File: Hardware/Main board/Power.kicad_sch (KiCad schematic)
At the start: 12 parts, among them U5 TLV1117-33, U6 TLV1117-33, U7 TLV1117-33, U8 TLV1117-33

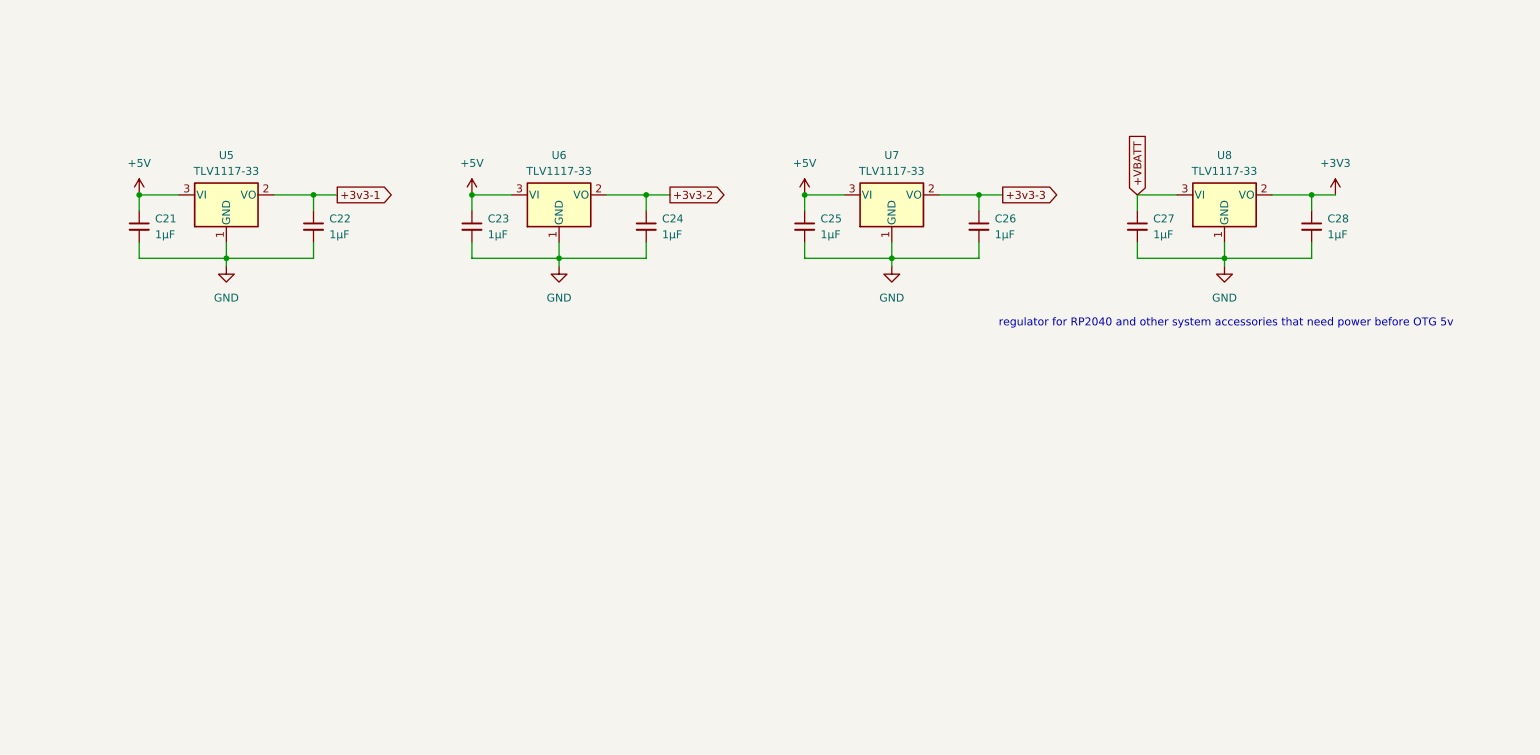
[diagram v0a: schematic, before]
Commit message: hardware changes and initial traces/layout
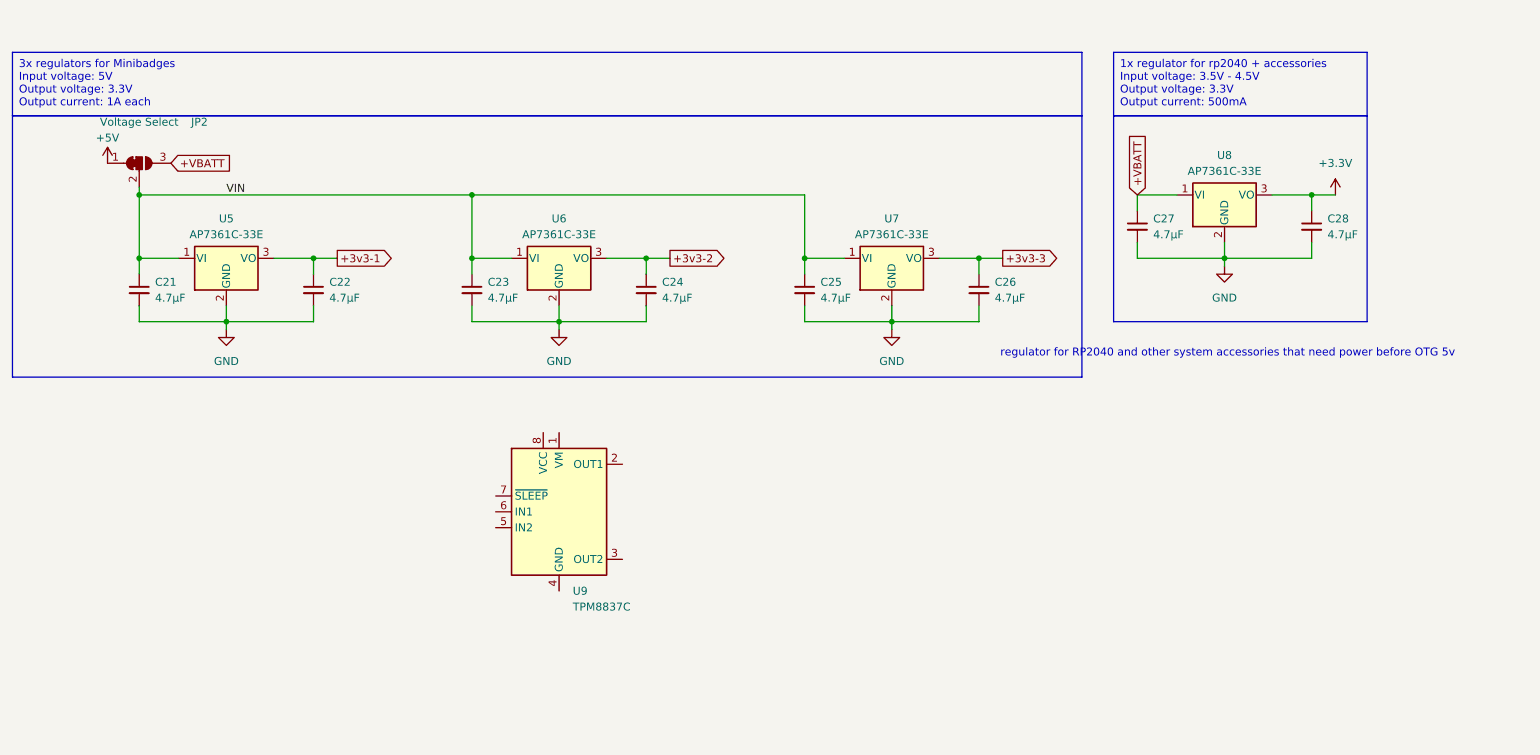
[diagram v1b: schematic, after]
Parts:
- added JP2: Voltage Select, Jumper:SolderJumper-3_P1.3mm_Bridged12_Pad1.0x1.5mm_NumberLabels, symbol Jumper:SolderJumper_3_Bridged12
- added U9: TPM8837C, Package_SO:SOIC-8_3.9x4.9mm_P1.27mm, symbol Driver_Motor:DRV8837C
- C21, C22, C23, C24, C25, C26, C27, C28: value 1μF -> 4.7μF; footprint (none) -> Capacitor_SMD:C_0603_1608Metric
- U5, U6, U7, U8: value TLV1117-33 -> AP7361C-33E; footprint (none) -> Package_TO_SOT_SMD:SOT-223-3_TabPin2; symbol Regulator_Linear:TLV1117-33 -> Regulator_Linear:AP7361C-33E
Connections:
- net +3v3-1: now also U5.3 (VO); no longer U5.2 (VO)
- net +3v3-2: now also U6.3 (VO); no longer U6.2 (VO)
- net +3v3-3: now also U7.3 (VO); no longer U7.2 (VO)
- net +5V: now also JP2.1 (A); no longer C21.1, C23.1, C25.1, U5.3 (VI), U6.3 (VI), U7.3 (VI)
- net +VBATT: now also U8.1 (VI), JP2.3 (B); no longer U8.3 (VI)
- net GND: now also U5.2 (GND), U6.2 (GND), U7.2 (GND), U8.2 (GND); no longer U5.1 (GND), U6.1 (GND), U7.1 (GND), U8.1 (GND)
- net +3V3 renamed +3.3V
- net +3.3V: now also U8.3 (VO); no longer U8.2 (VO)
- new net: U9.4 (GND), U9.9 (GND)
- new net VIN: C21.1, C23.1, C25.1, JP2.2 (C), U5.1 (VI), U6.1 (VI), U7.1 (VI)
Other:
- moved on the sheet: C21, C22, C23, C24, C25, C26, U5, U6, U7

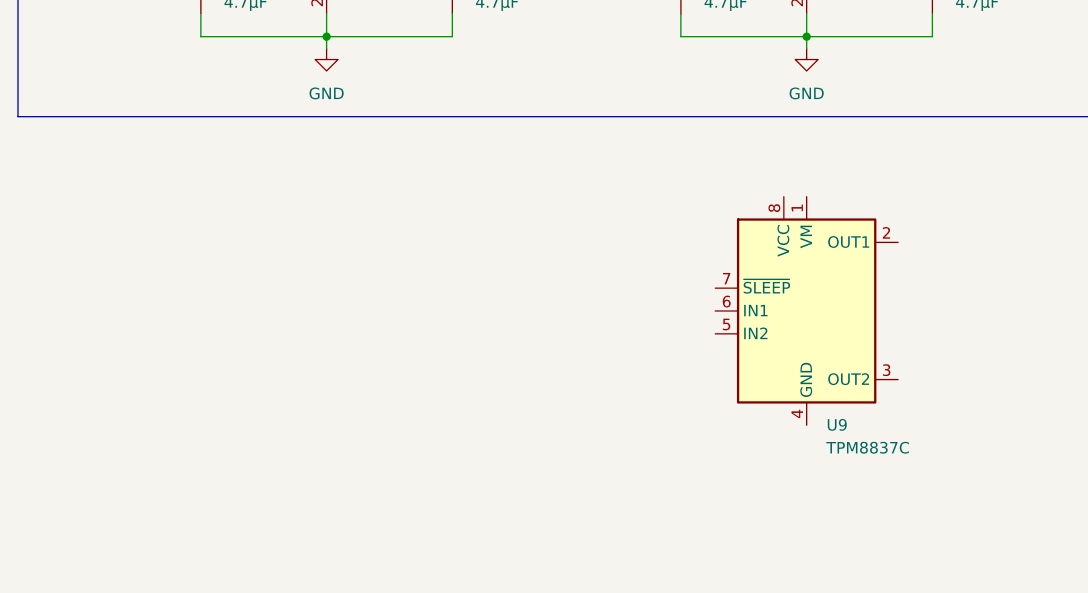
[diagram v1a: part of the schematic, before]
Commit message: update power for TPM
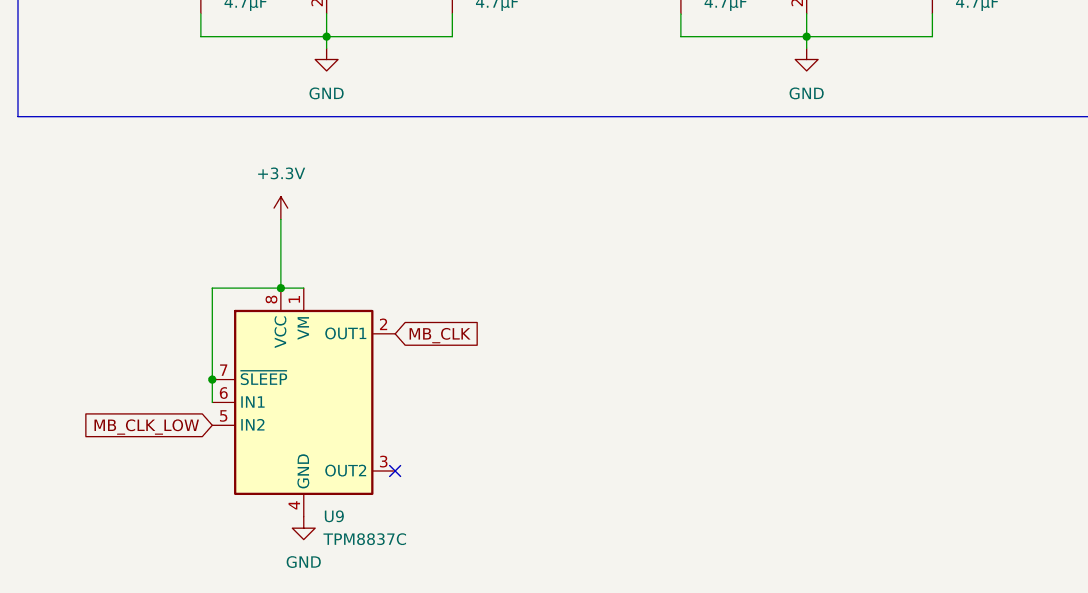
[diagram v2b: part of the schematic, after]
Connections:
- net +3.3V: now also U9.1 (VM), U9.6 (IN1), U9.7 (~{SLEEP}), U9.8 (VCC)
- net GND: now also U9.4 (GND), U9.9 (GND)
- net MB_CLK: now reaches U9.2 (OUT1)
- net MB_CLK_LOW: now reaches U9.5 (IN2)
- no-connect marks 0 -> 1
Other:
- moved on the sheet: U9
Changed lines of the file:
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@@
 	(paper "A4")
+	(junction
+		(at 49.53 113.03)
+		(diameter 0)
+		(color 0 0 0 0)
+	)
 	(junction
 		(at 129.54 64.77)
@@
 	)
 	(junction
+		(at 57.15 102.87)
+		(diameter 0)
+		(color 0 0 0 0)
+	)
+	(junction
 		(at 236.22 54.61)
 		(diameter 0)
@@
 		(color 0 0 0 0)
 	)
+	(no_connect
+		(at 69.85 123.19)
+	)
 	(wire
 		(pts
@@
 	(wire
 		(pts
+			(xy 49.53 113.03) (xy 49.53 115.57)
+		)
+		(stroke
+			(width 0)
+			(type default)
+		)
+	)
+	(wire
+		(pts
 			(xy 208.28 64.77) (xy 222.25 64.77)
 		)
@@
 	(wire
 		(pts
+			(xy 57.15 95.25) (xy 57.15 102.87)
+		)
+		(stroke
+			(width 0)
+			(type default)
+		)
+	)
+	(wire
+		(pts
 			(xy 154.94 54.61) (xy 154.94 64.77)
 		)
@@
 	(wire
 		(pts
+			(xy 57.15 102.87) (xy 59.69 102.87)
+		)
+		(stroke
+			(width 0)
+			(type default)
+		)
+	)
+	(wire
+		(pts
 			(xy 101.6 74.93) (xy 115.57 74.93)
 		)
@@
 	(wire
 		(pts
+			(xy 49.53 102.87) (xy 49.53 113.03)
+		)
+		(stroke
+			(width 0)
+			(type default)
+		)
+	)
+	(wire
+		(pts
 			(xy 76.2 72.39) (xy 76.2 74.93)
 		)
@@
 		(pts
 			(xy 236.22 64.77) (xy 222.25 64.77)
+		)
+		(stroke
+			(width 0)
+			(type default)
+		)
+	)
+	(wire
+		(pts
+			(xy 57.15 102.87) (xy 49.53 102.87)
 		)
 		(stroke
@@
 		)
 	)
+	(global_label "MB_CLK_LOW"
+		(shape input)
+		(at 49.53 118.11 180)
+		(fields_autoplaced yes)
+		(effects
+			(font
+				(size 1.27 1.27)
+			)
+			(justify right)
+		)
+		(property "Intersheetrefs" "${INTERSHEET_REFS}"
+			(at 34.5101 118.11 0)
+			(effects
+				(font
+					(size 1.27 1.27)
+				)
+				(justify right)
+				(hide yes)
+			)
+		)
+	)
 	(global_label "+3v3-1"
 		(shape output)
@@
 		(property "Intersheetrefs" "${INTERSHEET_REFS}"
 			(at 208.28 44.67 90)
+			(effects
+				(font
+					(size 1.27 1.27)
+				)
+				(justify left)
+				(hide yes)
+			)
+		)
+	)
+	(global_label "MB_CLK"
+		(shape input)
+		(at 69.85 107.95 0)
+		(fields_autoplaced yes)
+		(effects
+			(font
+				(size 1.27 1.27)
+			)
+			(justify left)
+		)
+		(property "Intersheetrefs" "${INTERSHEET_REFS}"
+			(at 80.0923 107.95 0)
 			(effects
 				(font
@@
 	)
 	(symbol
+		(lib_id "power:+3.3V")
+		(at 57.15 95.25 0)
+		(unit 1)
+		(exclude_from_sim no)
+		(in_bom yes)
+		(on_board yes)
+		(dnp no)
+		(fields_autoplaced yes)
+		(property "Reference" "#PWR044"
+			(at 57.15 99.06 0)
+			(effects
+				(font
+					(size 1.27 1.27)
+				)
+				(hide yes)
+			)
+		)
+		(property "Value" "+3.3V"
+			(at 57.15 90.17 0)
+			(effects
+				(font
+					(size 1.27 1.27)
+				)
+			)
+		)
+		(property "Footprint" ""
+			(at 57.15 95.25 0)
+			(effects
+				(font
+					(size 1.27 1.27)
+				)
+				(hide yes)
+			)
+		)
+		(property "Datasheet" ""
+			(at 57.15 95.25 0)
+			(effects
+				(font
+					(size 1.27 1.27)
+				)
+				(hide yes)
+			)
+		)
+		(property "Description" "Power symbol creates a global label with name \"+3.3V\""
+			(at 57.15 95.25 0)
+			(effects
+				(font
+					(size 1.27 1.27)
+				)
+				(hide yes)
+			)
+		)
+		(pin "1"
+		)
+		(instances
+			(project ""
+				(path "/e5119d15-74fb-4259-abbc-5cab1f368532/7829a1d4-1109-4ab0-9e3a-4c6d8c9e21fc"
+					(reference "#PWR044")
+					(unit 1)
+				)
+			)
+		)
+	)
+	(symbol
 		(lib_id "Jumper:SolderJumper_3_Bridged12")
 		(at 48.26 49.53 0)
@@
 	)
 	(symbol
+		(lib_id "power:GND")
+		(at 59.69 128.27 0)
+		(unit 1)
+		(exclude_from_sim no)
+		(in_bom yes)
+		(on_board yes)
+		(dnp no)
+		(fields_autoplaced yes)
+		(property "Reference" "#PWR045"
+			(at 59.69 134.62 0)
+			(effects
+				(font
+					(size 1.27 1.27)
+				)
+				(hide yes)
+			)
+		)
+		(property "Value" "GND"
+			(at 59.69 133.35 0)
+			(effects
+				(font
+					(size 1.27 1.27)
+				)
+			)
+		)
+		(property "Footprint" ""
+			(at 59.69 128.27 0)
+			(effects
+				(font
+					(size 1.27 1.27)
+				)
+				(hide yes)
+			)
+		)
+		(property "Datasheet" ""
+			(at 59.69 128.27 0)
+			(effects
+				(font
+					(size 1.27 1.27)
+				)
+				(hide yes)
+			)
+		)
+		(property "Description" "Power symbol creates a global label with name \"GND\" , ground"
+			(at 59.69 128.27 0)
+			(effects
+				(font
+					(size 1.27 1.27)
+				)
+				(hide yes)
+			)
+		)
+		(pin "1"
+		)
+		(instances
+			(project ""
+				(path "/e5119d15-74fb-4259-abbc-5cab1f368532/7829a1d4-1109-4ab0-9e3a-4c6d8c9e21fc"
+					(reference "#PWR045")
+					(unit 1)
+				)
+			)
+		)
+	)
+	(symbol
 		(lib_id "Device:C_Small")
 		(at 129.54 69.85 0)
@@
 	(symbol
 		(lib_id "Driver_Motor:DRV8837C")
-		(at 115.57 105.41 0)
+		(at 59.69 115.57 0)
 		(unit 1)
 		(exclude_from_sim no)
@@
 		(dnp no)
 		(property "Reference" "U9"
-			(at 117.7641 118.11 0)
+			(at 61.8841 128.27 0)
 			(effects
 				(font
@@
 		)
 		(property "Value" "TPM8837C"
-			(at 117.7641 120.65 0)
+			(at 61.8841 130.81 0)
 			(effects
 				(font
@@
 		)
 		(property "Footprint" "Package_SO:SOIC-8_3.9x4.9mm_P1.27mm"
-			(at 115.57 127 0)
+			(at 59.69 137.16 0)
 			(effects
 				(font
@@
 		)
 		(property "Datasheet" "http://www.ti.com/lit/ds/symlink/drv8837c.pdf"
-			(at 115.57 105.41 0)
+			(at 59.69 115.57 0)
 			(effects
 				(font
@@
 		)
 		(property "Description" "H-Bridge driver, 1A, Low Voltage, PWM input, WSON-8"
-			(at 115.57 105.41 0)
-			(effects
-				(font
+			(at 59.69 115.57 0)
+			(effects
+				(font

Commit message: Part selection
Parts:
- U5, U6, U7, U8: JLCPCB Part # (none) -> C500795; LCSC Part # (none) -> C500795
- U9: JLCPCB Part # (none) -> C7436831; LCSC Part # (none) -> C7436831
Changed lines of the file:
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@@
+			)
+		)
+		(property "JLCPCB Part #" "C500795"
+			(at 222.25 54.61 0)
+			(effects
+				(font
+					(size 1.27 1.27)
+				)
+				(hide yes)
+			)
+		)
+		(property "LCSC Part #" "C500795"
+			(at 222.25 54.61 0)
+			(effects
+				(font
+					(size 1.27 1.27)
+				)
+				(hide yes)
 			)
 		)
@@
 			)
 		)
+		(property "JLCPCB Part #" "C500795"
+			(at 168.91 64.77 0)
+			(effects
+				(font
+					(size 1.27 1.27)
+				)
+				(hide yes)
+			)
+		)
+		(property "LCSC Part #" "C500795"
+			(at 168.91 64.77 0)
+			(effects
+				(font
+					(size 1.27 1.27)
+				)
+				(hide yes)
+			)
+		)
 		(pin "3"
 		)
@@
 			)
 		)
+		(property "JLCPCB Part #" "C500795"
+			(at 62.23 64.77 0)
+			(effects
+				(font
+					(size 1.27 1.27)
+				)
+				(hide yes)
+			)
+		)
+		(property "LCSC Part #" "C500795"
+			(at 62.23 64.77 0)
+			(effects
+				(font
+					(size 1.27 1.27)
+				)
+				(hide yes)
+			)
+		)
 		(pin "3"
 		)
@@
 			)
 		)
+		(property "JLCPCB Part #" "C7436831"
+			(at 59.69 115.57 0)
+			(effects
+				(font
+					(size 1.27 1.27)
+				)
+				(hide yes)
+			)
+		)
+		(property "LCSC Part #" "C7436831"
+			(at 59.69 115.57 0)
+			(effects
+				(font
+					(size 1.27 1.27)
+				)
+				(hide yes)
+			)
+		)
 		(pin "8"
 		)
@@
 			(at 115.57 64.77 0)
 			(effects
+				(font
+					(size 1.27 1.27)
+				)
+				(hide yes)
+			)
+		)
+		(property "JLCPCB Part #" "C500795"
+			(at 115.57 64.77 0)
+			(effects
+				(font
+					(size 1.27 1.27)
+				)
+				(hide yes)
+			)
+		)
+		(property "LCSC Part #" "C500795"
+			(at 115.57 64.77 0)
+			(effects

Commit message: Reworking BMS
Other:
- moved on the sheet: U9
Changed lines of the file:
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@@
 	(paper "A4")
 	(junction
-		(at 49.53 113.03)
+		(at 59.69 118.11)
 		(diameter 0)
 		(color 0 0 0 0)
@@
 	)
 	(junction
-		(at 57.15 102.87)
+		(at 67.31 107.95)
 		(diameter 0)
 		(color 0 0 0 0)
@@
 	)
 	(no_connect
-		(at 69.85 123.19)
+		(at 80.01 128.27)
 	)
 	(wire
@@
 	(wire
 		(pts
-			(xy 49.53 113.03) (xy 49.53 115.57)
+			(xy 59.69 118.11) (xy 59.69 120.65)
 		)
 		(stroke
@@
 	(wire
 		(pts
-			(xy 57.15 95.25) (xy 57.15 102.87)
+			(xy 67.31 100.33) (xy 67.31 107.95)
 		)
 		(stroke
@@
 	(wire
 		(pts
-			(xy 57.15 102.87) (xy 59.69 102.87)
+			(xy 67.31 107.95) (xy 69.85 107.95)
 		)
 		(stroke
@@
 	(wire
 		(pts
-			(xy 49.53 102.87) (xy 49.53 113.03)
+			(xy 59.69 107.95) (xy 59.69 118.11)
 		)
 		(stroke
@@
 	(wire
 		(pts
-			(xy 57.15 102.87) (xy 49.53 102.87)
+			(xy 67.31 107.95) (xy 59.69 107.95)
 		)
 		(stroke
@@
 	(global_label "MB_CLK_LOW"
 		(shape input)
-		(at 49.53 118.11 180)
+		(at 59.69 123.19 180)
 		(fields_autoplaced yes)
 		(effects
@@
 		)
 		(property "Intersheetrefs" "${INTERSHEET_REFS}"
-			(at 34.5101 118.11 0)
+			(at 44.6701 123.19 0)
 			(effects
 				(font
@@
 	(global_label "MB_CLK"
 		(shape input)
-		(at 69.85 107.95 0)
+		(at 80.01 113.03 0)
 		(fields_autoplaced yes)
 		(effects
@@
 		)
 		(property "Intersheetrefs" "${INTERSHEET_REFS}"
-			(at 80.0923 107.95 0)
+			(at 90.2523 113.03 0)
 			(effects
 				(font
@@
 			)
 		)
+		(property "Design guide" ""
+			(at 101.6 69.85 0)
+			(effects
+				(font
+					(size 1.27 1.27)
+				)
+				(hide yes)
+			)
+		)
 		(pin "1"
 		)
@@
 			)
 		)
+		(property "Design guide" ""
+			(at 236.22 59.69 0)
+			(effects
+				(font
+					(size 1.27 1.27)
+				)
+				(hide yes)
+			)
+		)
 		(pin "1"
 		)
@@
 		)
 		(property "LCSC Part #" "C500795"
+			(at 222.25 54.61 0)
+			(effects
+				(font
+					(size 1.27 1.27)
+				)
+				(hide yes)
+			)
+		)
+		(property "Design guide" ""
 			(at 222.25 54.61 0)
 			(effects
@@
 			)
 		)
+		(property "Design guide" ""
+			(at 76.2 69.85 0)
+			(effects
+				(font
+					(size 1.27 1.27)
+				)
+				(hide yes)
+			)
+		)
 		(pin "1"
 		)
@@
 			)
 		)
+		(property "Design guide" ""
+			(at 48.26 69.85 0)
+			(effects
+				(font
+					(size 1.27 1.27)
+				)
+				(hide yes)
+			)
+		)
 		(pin "1"
 		)
@@
 	(symbol
 		(lib_id "power:+3.3V")
-		(at 57.15 95.25 0)
+		(at 67.31 100.33 0)
 		(unit 1)
 		(exclude_from_sim no)
@@
 		(fields_autoplaced yes)
 		(property "Reference" "#PWR044"
-			(at 57.15 99.06 0)
+			(at 67.31 104.14 0)
 			(effects
 				(font
@@
 		)
 		(property "Value" "+3.3V"
-			(at 57.15 90.17 0)
+			(at 67.31 95.25 0)
 			(effects
 				(font
@@
 		)
 		(property "Footprint" ""
-			(at 57.15 95.25 0)
+			(at 67.31 100.33 0)
 			(effects
 				(font
@@
 		)
 		(property "Datasheet" ""
-			(at 57.15 95.25 0)
+			(at 67.31 100.33 0)
 			(effects
 				(font
@@
 		)
 		(property "Description" "Power symbol creates a global label with name \"+3.3V\""
-			(at 57.15 95.25 0)
+			(at 67.31 100.33 0)
 			(effects
 				(font
@@
 			)
 		)
+		(property "Design guide" ""
+			(at 48.26 49.53 0)
+			(effects
+				(font
+					(size 1.27 1.27)
+				)
+				(hide yes)
+			)
+		)
 		(pin "1"
 		)
@@
 			)
 		)
+		(property "Design guide" ""
+			(at 208.28 59.69 0)
+			(effects
+				(font
+					(size 1.27 1.27)
+				)
+				(hide yes)
+			)
+		)
 		(pin "1"
 		)
@@
 			)
 		)
+		(property "Design guide" ""
+			(at 168.91 64.77 0)
+			(effects
+				(font
+					(size 1.27 1.27)
+				)
+				(hide yes)
+			)
+		)
 		(pin "3"
 		)
@@
 			)
 		)
+		(property "Design guide" ""
+			(at 182.88 69.85 0)
+			(effects
+				(font
+					(size 1.27 1.27)
+				)
+				(hide yes)
+			)
+		)
 		(pin "1"
 		)
@@
 			)
 		)
+		(property "Design guide" ""
+			(at 62.23 64.77 0)
+			(effects
+				(font
+					(size 1.27 1.27)
+				)
+				(hide yes)
+			)
+		)
 		(pin "3"
 		)
@@
 	(symbol
 		(lib_id "power:GND")
-		(at 59.69 128.27 0)
+		(at 69.85 133.35 0)
 		(unit 1)
 		(exclude_from_sim no)
@@
 		(fields_autoplaced yes)
 		(property "Reference" "#PWR045"
-			(at 59.69 134.62 0)
+			(at 69.85 139.7 0)
 			(effects
 				(font
@@
 		)
 		(property "Value" "GND"
-			(at 59.69 133.35 0)
+			(at 69.85 138.43 0)
 			(effects
 				(font
@@
 		)
 		(property "Footprint" ""
-			(at 59.69 128.27 0)
+			(at 69.85 133.35 0)
 			(effects
 				(font
@@
 		)
 		(property "Datasheet" ""
-			(at 59.69 128.27 0)
+			(at 69.85 133.35 0)
 			(effects
 				(font
@@
 		)
 		(property "Description" "Power symbol creates a global label with name \"GND\" , ground"
-			(at 59.69 128.27 0)
+			(at 69.85 133.35 0)
 			(effects
 				(font
@@
 			)
 		)
+		(property "Design guide" ""
+			(at 129.54 69.85 0)
+			(effects
+				(font
+					(size 1.27 1.27)
+				)
+				(hide yes)
+			)
+		)
 		(pin "1"
 		)
@@
 	(symbol
 		(lib_id "Driver_Motor:DRV8837C")
-		(at 59.69 115.57 0)
+		(at 69.85 120.65 0)
 		(unit 1)
 		(exclude_from_sim no)
@@
 		(dnp no)
 		(property "Reference" "U9"
-			(at 61.8841 128.27 0)
+			(at 72.0441 133.35 0)
 			(effects
 				(font
@@
 		)
 		(property "Value" "TPM8837C"
-			(at 61.8841 130.81 0)
+			(at 72.0441 135.89 0)
 			(effects
 				(font
@@
 		)
 		(property "Footprint" "Package_SO:SOIC-8_3.9x4.9mm_P1.27mm"
-			(at 59.69 137.16 0)
+			(at 69.85 142.24 0)
 			(effects
 				(font
@@
 		)
 		(property "Datasheet" "http://www.ti.com/lit/ds/symlink/drv8837c.pdf"
-			(at 59.69 115.57 0)
+			(at 69.85 120.65 0)
 			(effects
 				(font
@@
 		)
 		(property "Description" "H-Bridge driver, 1A, Low Voltage, PWM input, WSON-8"
-			(at 59.69 115.57 0)
+			(at 69.85 120.65 0)
 			(effects
 				(font
@@
 		)
 		(property "JLCPCB Part #" "C7436831"
-			(at 59.69 115.57 0)
+			(at 69.85 120.65 0)
 			(effects
 				(font
@@
 		)
 		(property "LCSC Part #" "C7436831"
-			(at 59.69 115.57 0)
+			(at 69.85 120.65 0)
+			(effects
+				(font
+					(size 1.27 1.27)
+				)
+				(hide yes)
+			)
+		)
+		(property "Design guide" ""
+			(at 69.85 120.65 0)
 			(effects
 				(font
@@
 			)
 		)
+		(property "Design guide" ""
+			(at 154.94 69.85 0)
+			(effects
+				(font
+					(size 1.27 1.27)
+				)
+				(hide yes)
+			)
+		)
 		(pin "1"
 		)
@@
 			(at 115.57 64.77 0)
 			(effects
+				(font
+					(size 1.27 1.27)
+				)
+				(hide yes)
+			)
+		)
+		(property "Design guide" ""
+			(at 115.57 64.77 0)
+			(effects
